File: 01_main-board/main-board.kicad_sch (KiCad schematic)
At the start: 1 part, among them U1 STM32F405RGTx

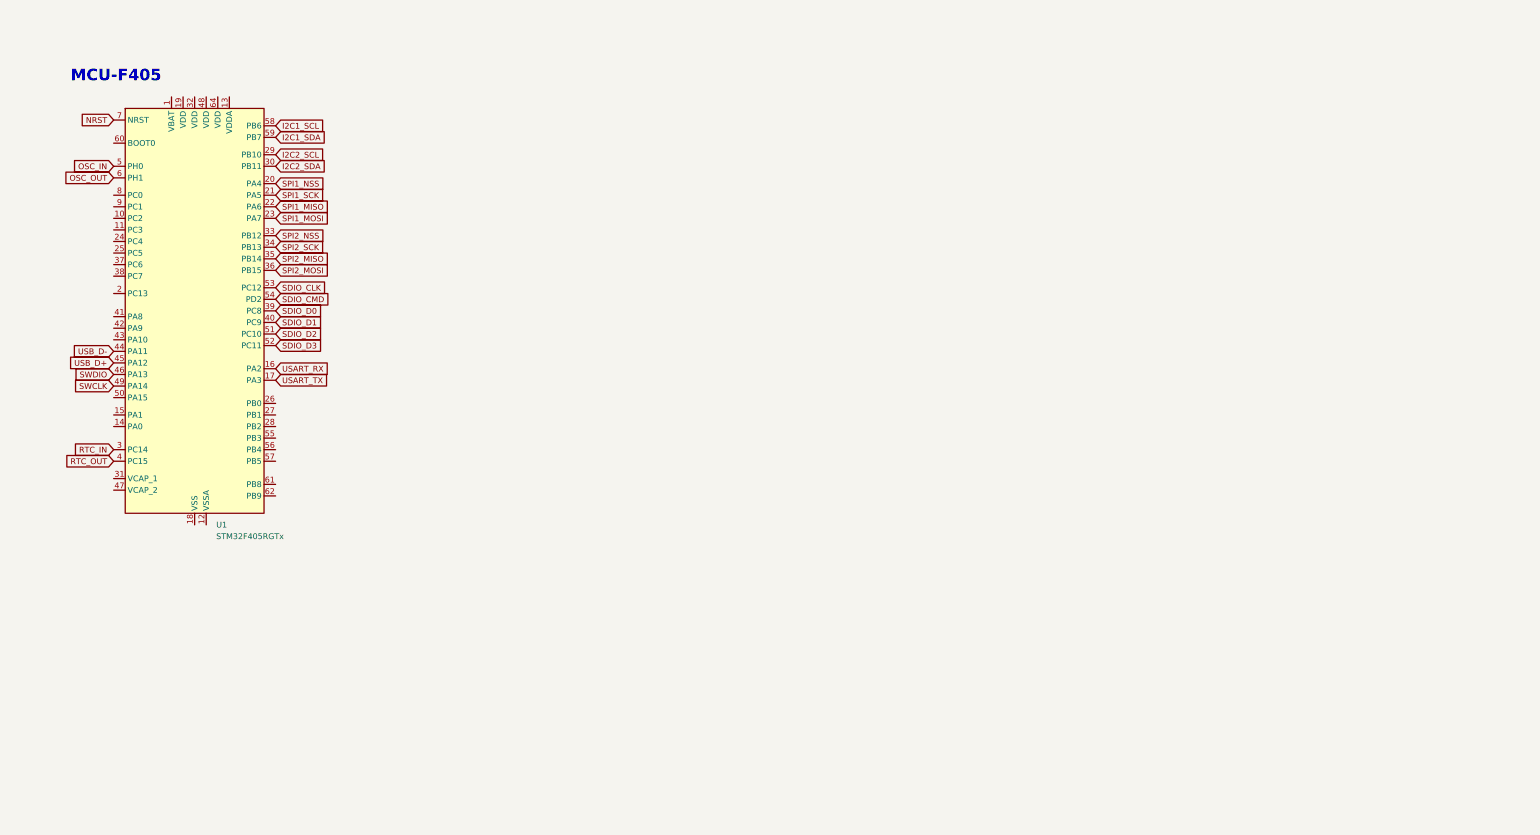
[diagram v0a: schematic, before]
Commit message: Added supporting circuitry
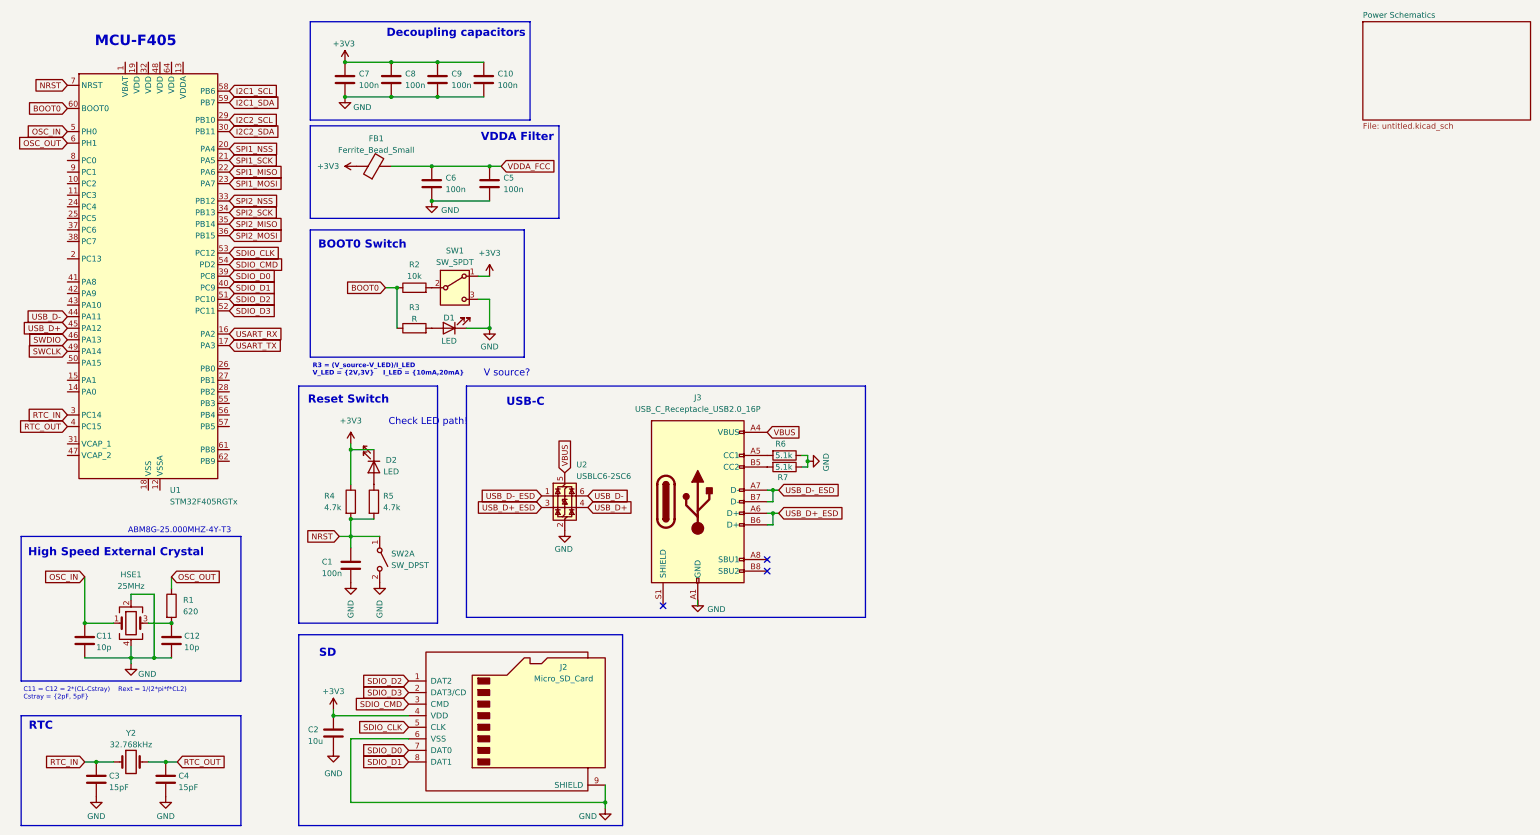
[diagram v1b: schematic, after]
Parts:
- added C1, C10, C5, C6, C7, C8, C9: 100n, symbol Device:C
- added C11, C12: 10p, symbol Device:C
- added C2: 10u, symbol Device:C
- added C3, C4: 15pF, symbol Device:C
- added D1, D2: LED, symbol Device:LED
- added FB1: Ferrite_Bead_Small, symbol Device:FerriteBead
- added HSE1: 25MHz, symbol Device:Crystal_GND24
- added J2: Micro_SD_Card, symbol Connector:Micro_SD_Card
- added J3: USB_C_Receptacle_USB2.0_16P, symbol Connector:USB_C_Receptacle_USB2.0_16P
- added R1: 620, symbol Device:R
- added R2: 10k, symbol Device:R
- added R3: R, symbol Device:R
- added R4, R5: 4.7k, symbol Device:R
- added R6, R7: 5.1k, symbol Device:R
- added SW1: SW_SPDT, symbol Switch:SW_SPDT
- added SW2: SW_DPST, symbol Switch:SW_DPST_x2
- added U2: USBLC6-2SC6, Package_TO_SOT_SMD:SOT-23-6, symbol Power_Protection:USBLC6-2SC6
- added Y2: 32.768kHz, symbol Device:Crystal
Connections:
- net NRST: now also C1.1, R4.2, R5.2, SW2.1 (A)
- net OSC_IN: now also C11.1, HSE1.1
- net OSC_OUT: now also R1.1
- net RTC_IN: now also C3.1, Y2.1
- net RTC_OUT: now also C4.1, Y2.2
- net SDIO_CLK: now also J2.5 (CLK)
- net SDIO_CMD: now also J2.3 (CMD)
- net SDIO_D0: now also J2.7 (DAT0)
- net SDIO_D1: now also J2.8 (DAT1)
- net SDIO_D2: now also J2.1 (DAT2)
- net SDIO_D3: now also J2.2 (DAT3/CD)
- net USB_D+: now also U2.4 (I/O2)
- net USB_D-: now also U2.6 (I/O1)
- net BOOT0: now reaches U1.60 (BOOT0)
- net BOOT0: now also R2.1, R3.1
- new net: J3.B5 (CC2), R7.2
- new net: C12.1, HSE1.3, R1.2
- new net: D2.2 (A), R5.1
- new net: D1.2 (A), R3.2
- new net: R2.2, SW1.2 (B)
- new net: J3.A5 (CC1), R6.2
- new net +3V3: C10.1, C2.1, C7.1, C8.1, C9.1, D2.1 (K), FB1.1, J2.4 (VDD), R4.1, SW1.1 (A)
- new net GND: C1.2, C10.2, C11.2, C12.2, C2.2, C3.2, C4.2, C5.2, C6.2, C7.2, C8.2, C9.2, D1.1 (K), HSE1.2, HSE1.4, J2.6 (VSS), J2.9 (SHIELD), J3.A1 (GND), J3.A12 (GND), J3.B1 (GND), J3.B12 (GND), R6.1, R7.1, SW1.3 (C), SW2.2 (B), U2.2 (GND)
- new net USB_D+_ESD: J3.A6 (D+), J3.B6 (D+), U2.3 (I/O2)
- new net USB_D-_ESD: J3.A7 (D-), J3.B7 (D-), U2.1 (I/O1)
- new net VBUS: J3.A4 (VBUS), J3.A9 (VBUS), J3.B4 (VBUS), J3.B9 (VBUS), U2.5 (VBUS)
- new net VDDA_FCC: C5.1, C6.1, FB1.2
- no-connect marks 0 -> 3
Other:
- added sheet Power Schematics (untitled.kicad_sch)
- note added: "ABM8G-25.000MHZ-4Y-T3"
- note added: "BOOT0 Switch"
- note added: "C11 = C12 = 2*(CL-Cstray) Rext = 1/(2*pi*f*CL2) Cstray = {2pF, 5pF}"
- note added: "Check LED path!"
- note added: "Decoupling capacitors"
- note added: "High Speed External Crystal"
- note added: "R3 = (V_source-V_LED)/I_LED V_LED = {2V,3V} I_LED = {10mA,20mA}"
- note added: "RTC"
- note added: "Reset Switch"
- note added: "SD"
- note added: "USB-C"
- note added: "V source?"
- note added: "VDDA Filter"
- moved on the sheet: U1
